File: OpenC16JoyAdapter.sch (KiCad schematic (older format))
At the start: 8 parts, among them J1 DB9_MALE, J2 TO_C16_MINI_DIN_8, SW1 PIN5_POWER, U1 74LS244

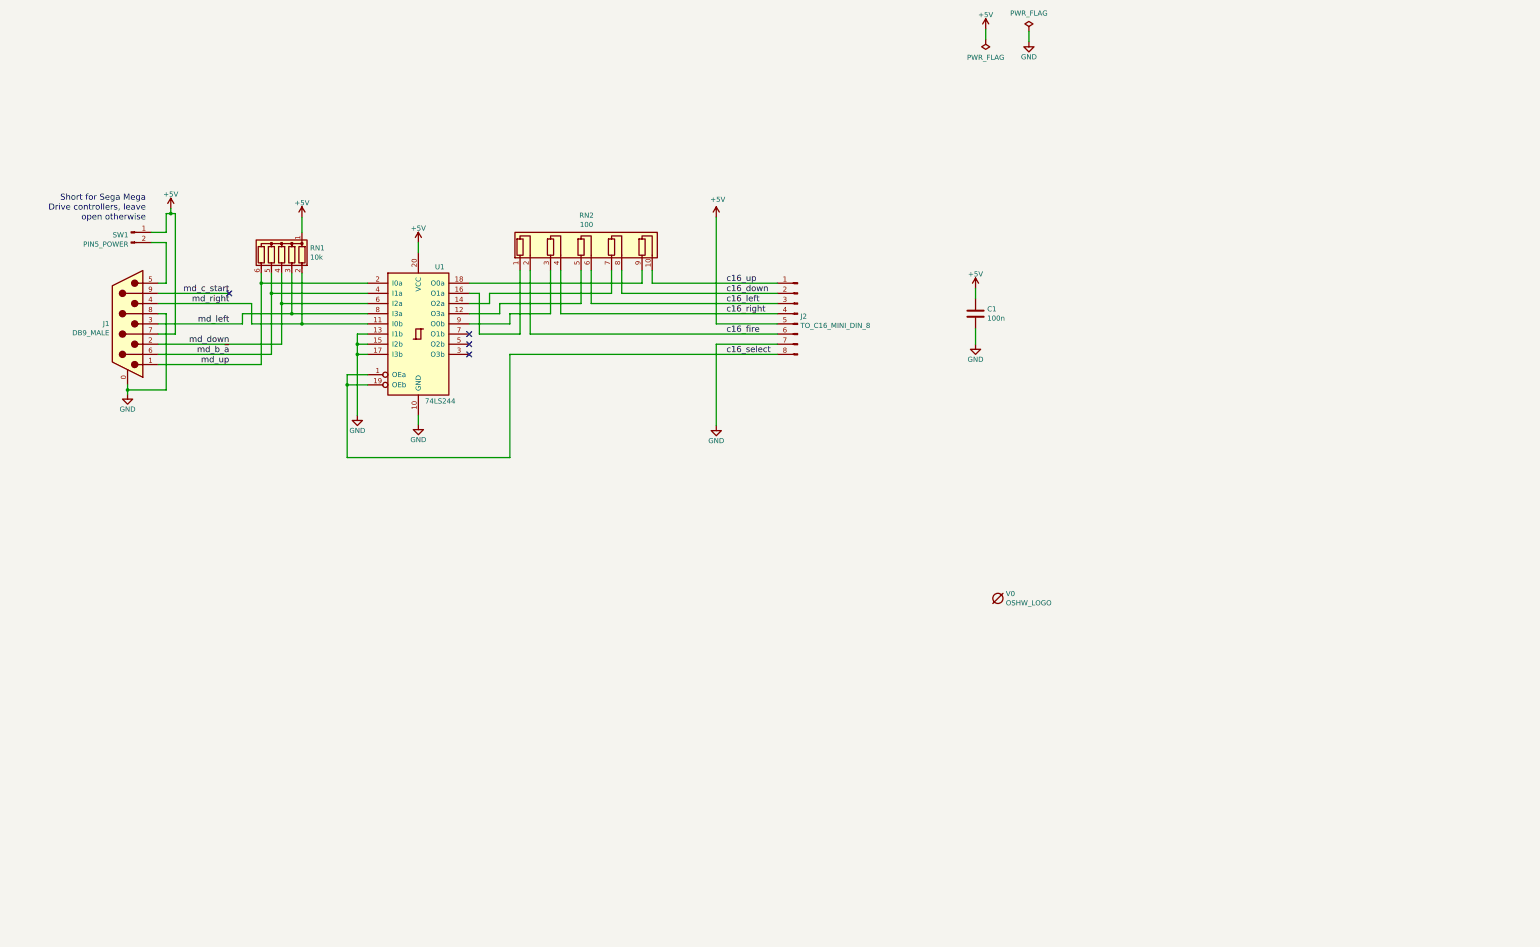
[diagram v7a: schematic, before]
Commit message: Integrate light pen circuit
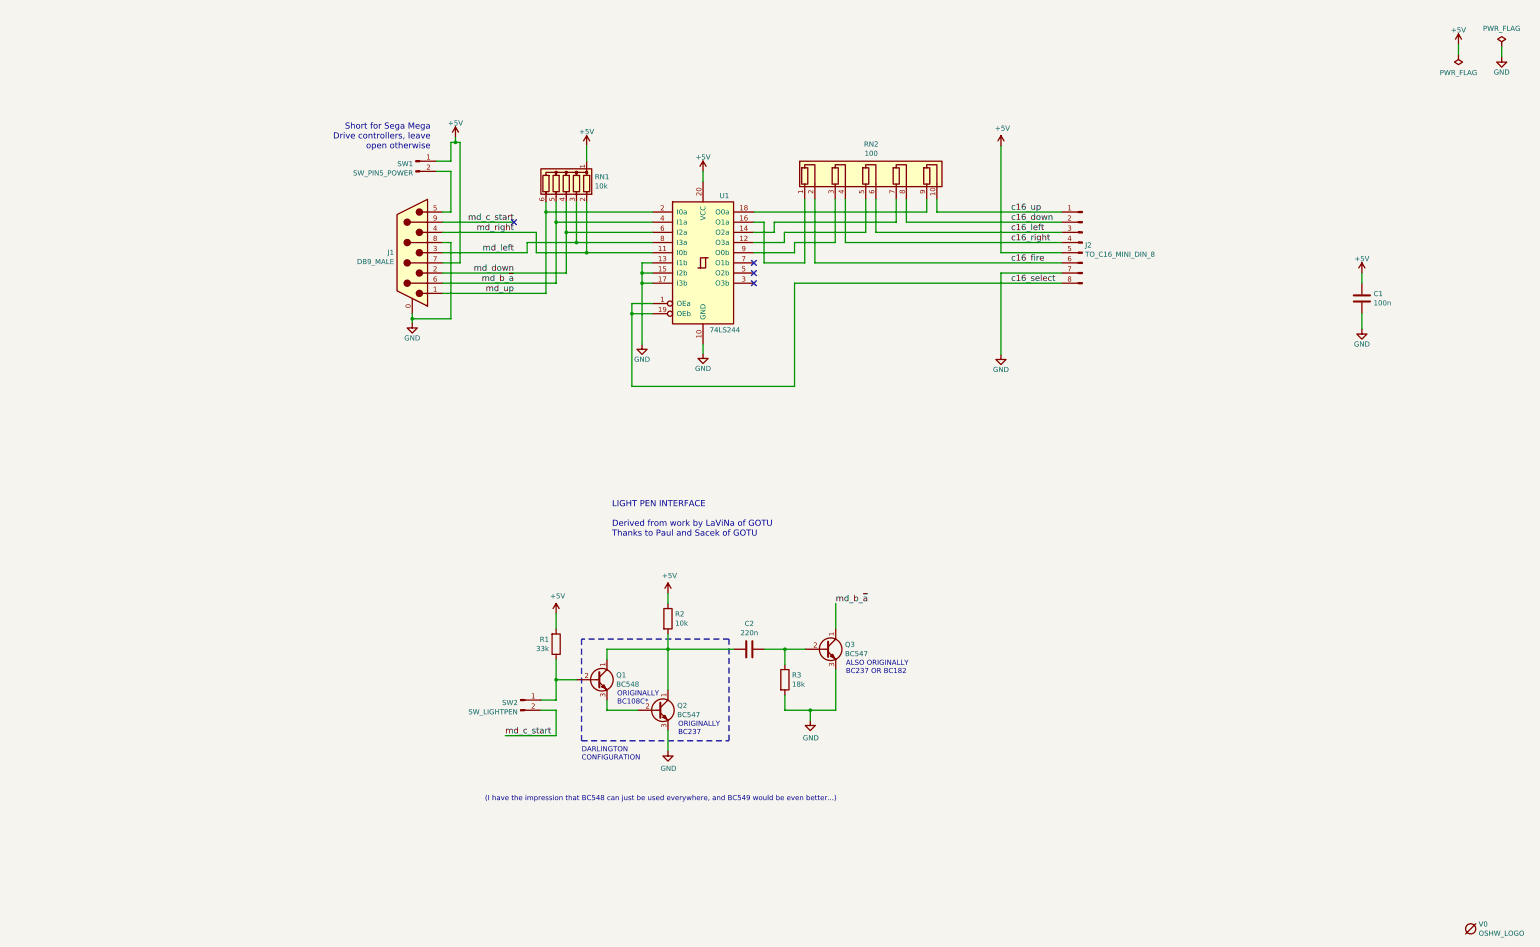
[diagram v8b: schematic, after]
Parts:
- added C2: 220n, Capacitor_THT:C_Disc_D7.0mm_W2.5mm_P5.00mm, symbol Device:C
- added Q1: BC548, Package_TO_SOT_THT:TO-92_HandSolder, symbol Transistor_BJT:BC548
- added Q2, Q3: BC547, Package_TO_SOT_THT:TO-92_HandSolder, symbol Transistor_BJT:BC547
- added R1: 33k, Resistor_THT:R_Axial_DIN0207_L6.3mm_D2.5mm_P2.54mm_Vertical, symbol Device:R
- added R2: 10k, Resistor_THT:R_Axial_DIN0207_L6.3mm_D2.5mm_P2.54mm_Vertical, symbol Device:R
- added R3: 18k, Resistor_THT:R_Axial_DIN0207_L6.3mm_D2.5mm_P2.54mm_Vertical, symbol Device:R
- added SW2: SW_LIGHTPEN, Connector_PinHeader_2.54mm:PinHeader_1x02_P2.54mm_Vertical, symbol Connector:Conn_01x02_Male
- SW1: value PIN5_POWER -> SW_PIN5_POWER
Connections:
- net +5V: now also R1.2, R2.1
- net GND: now also Q2.3 (E), Q3.3 (E), R3.2
- net md_b_~a: now also Q3.1 (C)
- net md_c_start: now also SW2.2 (Pin_2)
- new net: C2.2, Q1.1 (C), Q2.1 (C), R2.2
- new net: C2.1, Q3.2 (B), R3.1
- new net: Q1.2 (B), R1.1, SW2.1 (Pin_1)
- new net: Q1.3 (E), Q2.2 (B)
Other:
- note added: "(I have the impression that BC548 can just be used everywhere, and BC549 would be even better...)"
- note added: "ALSO ORIGINALLY\nBC237 OR BC182"
- note added: "DARLINGTON\nCONFIGURATION"
- note added: "LIGHT PEN INTERFACE\n\nDerived from work by LaViNa of GOTU\nThanks to Paul and Sacek of GOTU"
- note added: "ORIGINALLY\nBC108C*"
- note added: "ORIGINALLY\nBC237"
- moved on the sheet: C1, J1, J2, RN1, RN2, SW1, U1, V0
